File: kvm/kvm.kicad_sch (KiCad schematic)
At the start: 37 parts, among them J1 USB_C_Receptacle_USB2.0, J2 USB_C_Receptacle_USB2.0, SW1 SW_DPDT_x2, U1 FSUSB42MUX, U2 LTC4412xS6, U3 GL850G, U4 L78L33_SOT89, U5 SRV05-4

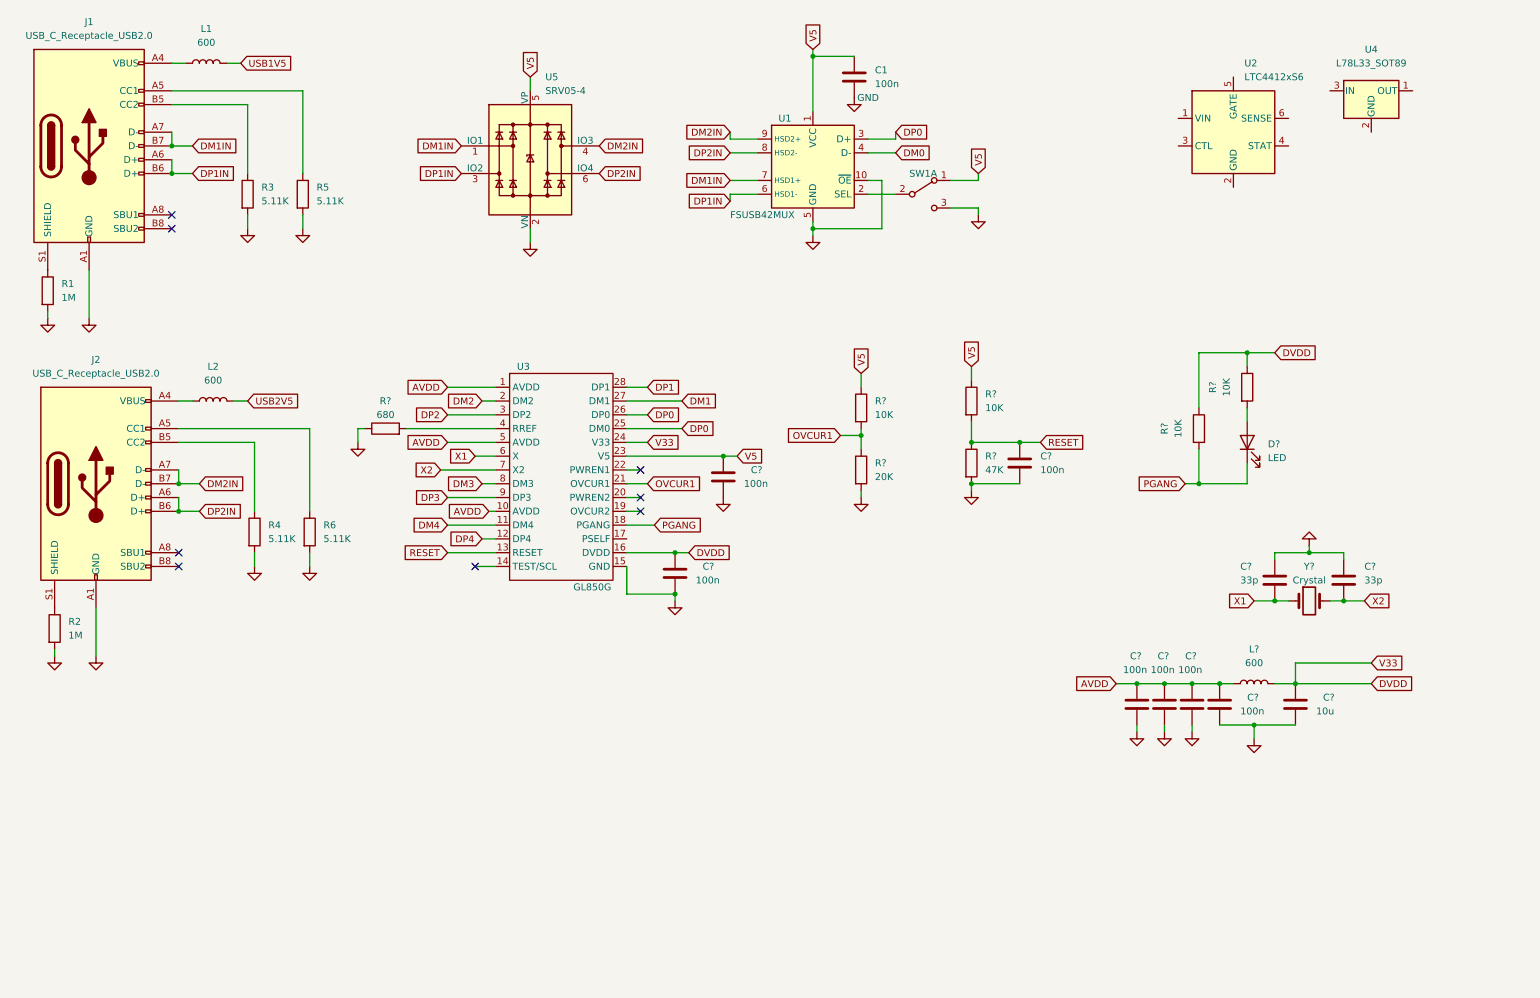
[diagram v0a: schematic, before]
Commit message: SCH: output side finished
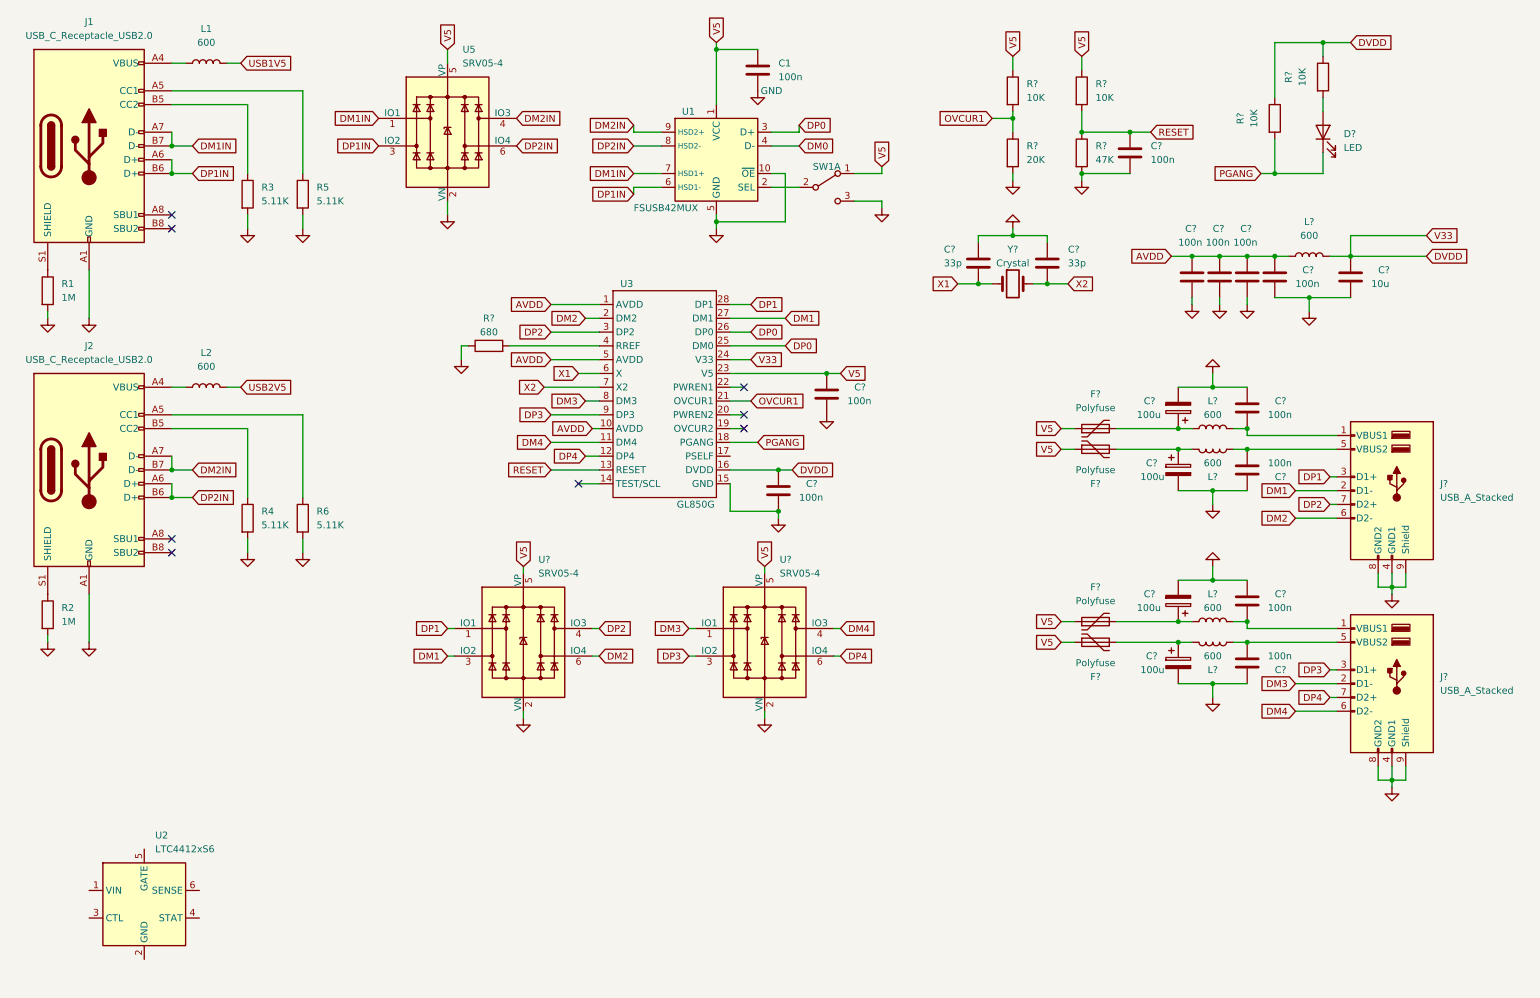
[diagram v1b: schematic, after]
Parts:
- removed U4: L78L33_SOT89, Package_TO_SOT_SMD:SOT-89-3, symbol Regulator_Linear:L78L33_SOT89
- added C? (x4): 100n, Capacitor_SMD:C_0603_1608Metric_Pad1.08x0.95mm_HandSolder, symbol Device:C
- added C? (x4): 100u, Capacitor_THT:CP_Radial_D5.0mm_P2.00mm, symbol Device:C_Polarized
- added F? (x4): Polyfuse, Fuse:Fuse_1206_3216Metric_Pad1.42x1.75mm_HandSolder, symbol Device:Polyfuse
- added J? (x2): USB_A_Stacked, symbol Connector:USB_A_Stacked
- added L? (x4): 600, Resistor_SMD:R_0603_1608Metric_Pad0.98x0.95mm_HandSolder, symbol Device:L
- added U? (x2): SRV05-4, Package_TO_SOT_SMD:SOT-23-6, symbol Power_Protection:SRV05-4
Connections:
- net DM1: now also J?.2 (D1-), U?.3 (IO2)
- net DM2: now also J?.6 (D2-), U?.6 (IO4)
- net DM3: now also J?.2 (D1-), U?.1 (IO1)
- net DM4: now also J?.6 (D2-), U?.4 (IO3)
- net DP1: now also J?.3 (D1+), U?.1 (IO1)
- net DP2: now also J?.7 (D2+), U?.4 (IO3)
- net DP3: now also J?.3 (D1+), U?.3 (IO2)
- net DP4: now also J?.7 (D2+), U?.6 (IO4)
- net GND: now also C?.1, C?.1, C?.1, C?.1, C?.2, C?.2, C?.2, C?.2, J?.4 (GND1), J?.4 (GND1), J?.8 (GND2), J?.8 (GND2), J?.9 (Shield), J?.9 (Shield), U?.2 (VN), U?.2 (VN)
- net V5: now also F?.1, F?.1, F?.1, F?.1, U?.5 (VP), U?.5 (VP)
- new net: C?.1, F?.2, L?.1 (x4)
- new net: C?.2, J?.1 (VBUS1), L?.2 (x2)
- new net: C?.2, J?.5 (VBUS2), L?.2 (x2)
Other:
- moved on the sheet: C1, C?, D?, J2, L2, L?, R2, R4, R6, R?, SW1A, U1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

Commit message: schematic done, footprints missing
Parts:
- added C2: 100u, Capacitor_THT:CP_Radial_D5.0mm_P2.00mm, symbol Device:C_Polarized
- added C3: 100n, Capacitor_SMD:C_0603_1608Metric_Pad1.08x0.95mm_HandSolder, symbol Device:C
- added D1: D_Schottky, Diode_SMD:D_SOD-123F, symbol Device:D_Schottky
- added M1: MPMOS, Package_TO_SOT_SMD:SOT-23-3, symbol pspice:MPMOS
- J1, J2: footprint (none) -> Connector_USB:USB_C_Receptacle_GCT_USB4085
- J3, J4: renamed from J?; footprint (none) -> Connector_USB:USB_A_Wuerth_61400826021_Horizontal_Stacked
- R12: renamed from R?; value 10K -> 100k
- R13: renamed from R?; value 10K -> 780
- SW1: footprint (none) -> Connector_PinHeader_2.54mm:PinHeader_1x03_P2.54mm_Vertical
- gave numbers to parts that had none: 36
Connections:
- net GND: now also U2.2 (GND), U2.3 (CTL), C2.2, C3.1
- net USB1V5: now also D1.2 (A)
- net USB2V5: now also U2.1 (VIN), M1.1 (D)
- net V5: now also U2.6 (SENSE), U3.17 (PSELF), C2.1, C3.2, D1.1 (K), M1.3 (S), M1.4 (B)
- net at U2.5 (GATE): now also M1.2 (G)
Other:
- moved on the sheet: U2

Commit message: finished schematic
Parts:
- removed M1: MPMOS, Package_TO_SOT_SMD:SOT-23-3, symbol pspice:MPMOS
- added Q1: Q_PMOS_GSD, Package_TO_SOT_SMD:SOT-23-3, symbol Device:Q_PMOS_GSD
- added R14: 470K, Resistor_SMD:R_0603_1608Metric_Pad0.98x0.95mm_HandSolder, symbol Device:R
- U3: footprint (none) -> Package_SO:SSOP-28_5.3x10.2mm_P0.65mm
- Y1: footprint (none) -> Library:ECS120184XCKM
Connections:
- net DM0: now also U3.25 (DM0)
- net DM1IN: now also U1.6 (HSD1-); no longer U1.7 (HSD1+)
- net DM2IN: now also U1.8 (HSD2-); no longer U1.9 (HSD2+)
- net DP0: no longer U3.25 (DM0)
- net DP1IN: now also U1.7 (HSD1+); no longer U1.6 (HSD1-)
- net DP2IN: now also U1.9 (HSD2+); no longer U1.8 (HSD2-)
- net USB2V5: now also Q1.3 (D)
- net V5: now also Q1.2 (S), R14.2
- net at U2.4 (STAT): now also R14.1
- net gate: now reaches U2.5 (GATE)
- net gate: now also Q1.1 (G)

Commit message: first layout version
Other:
- moved on the sheet: U4, U6

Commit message: first pcb layout
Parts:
- renumbered C3 to C1, C5 to C10, C4 to C11, C20 to C12, C8 to C13, C18 to C14, C19 to C15, C12 to C16, C11 to C17, C6 to C18, C13 to C19, C1 to C2, C7 to C20, C14 to C21, C2 to C3, C10 to C4, C17 to C5, C9 to C6, C16 to C7, C15 to C8, C21 to C9, F2 to F1, F1 to F2, F4 to F3, F3 to F4, L7 to L5, L5 to L7, R6 to R1, R4 to R10, R7 to R11, R10 to R13, R11 to R14, R14 to R2, R5 to R3, R1 to R4, R2 to R5, R3 to R6, R8 to R7, R9 to R8, R13 to R9, U5 to U2, U2 to U3, U3 to U4, U4 to U5
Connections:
- net DM0 renamed D0-
- net DM1 renamed D1-
- net DM1IN renamed D1IN-
- net DM2 renamed D2-
- net DM2IN renamed D2IN-
- net DM3 renamed D3-
- net DM4 renamed D4-
- net DP0 renamed D0+
- net DP1 renamed D1+
- net DP1IN renamed D1IN+
- net DP2 renamed D2+
- net DP2IN renamed D2IN+
- net DP3 renamed D3+
- net DP4 renamed D4+

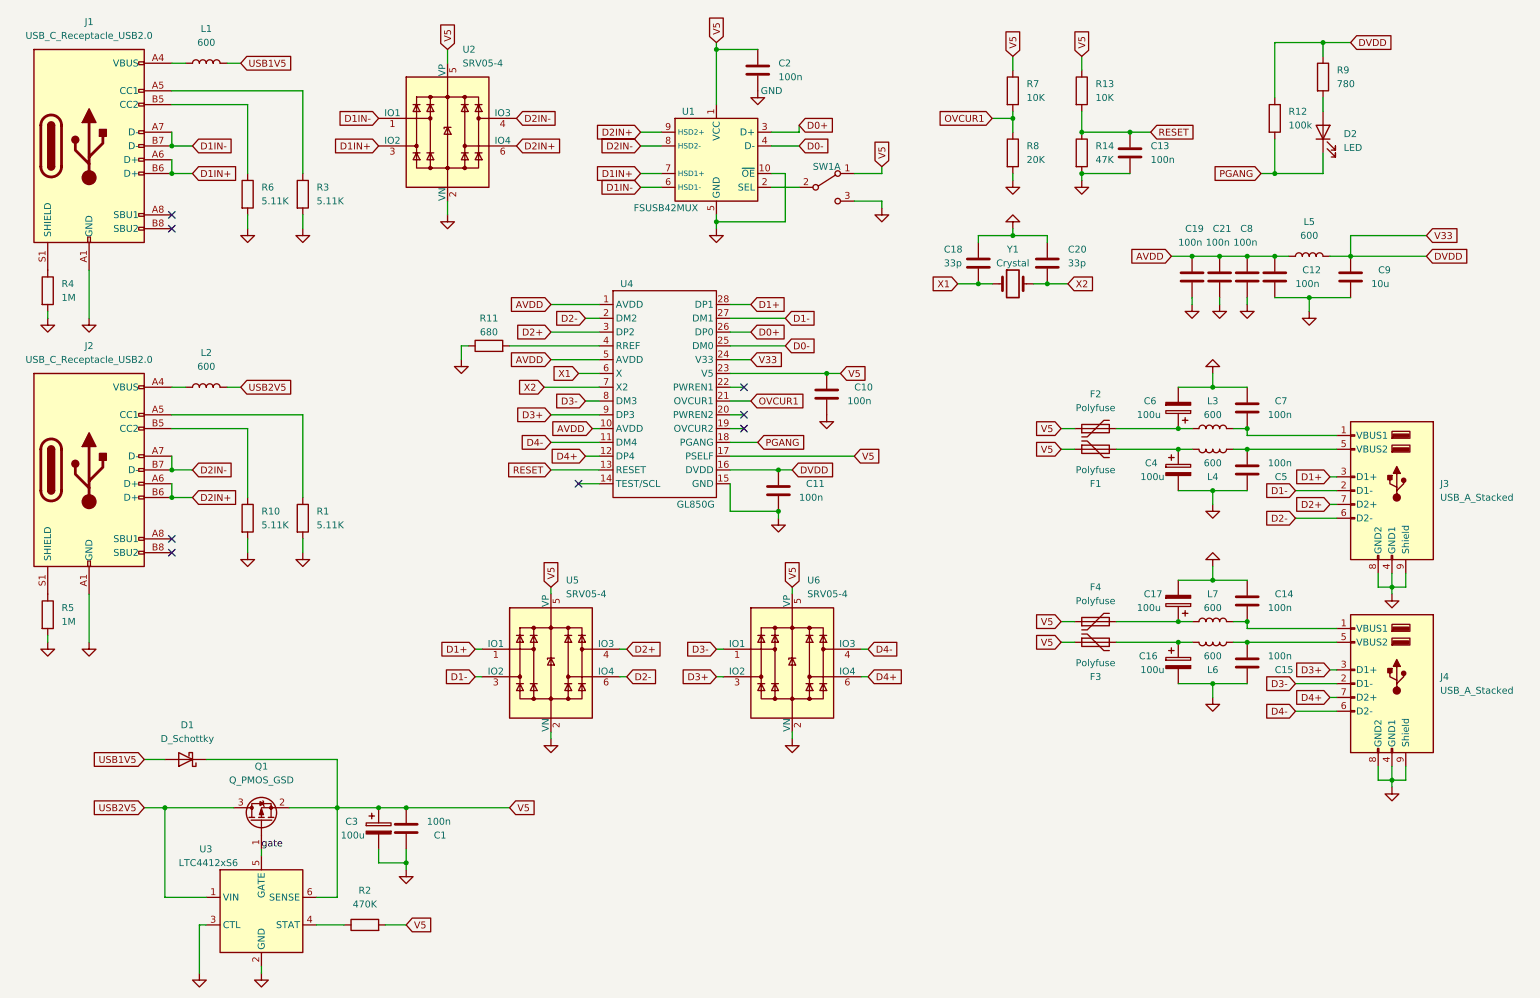
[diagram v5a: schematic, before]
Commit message: replaced USB-C ports with smd parts
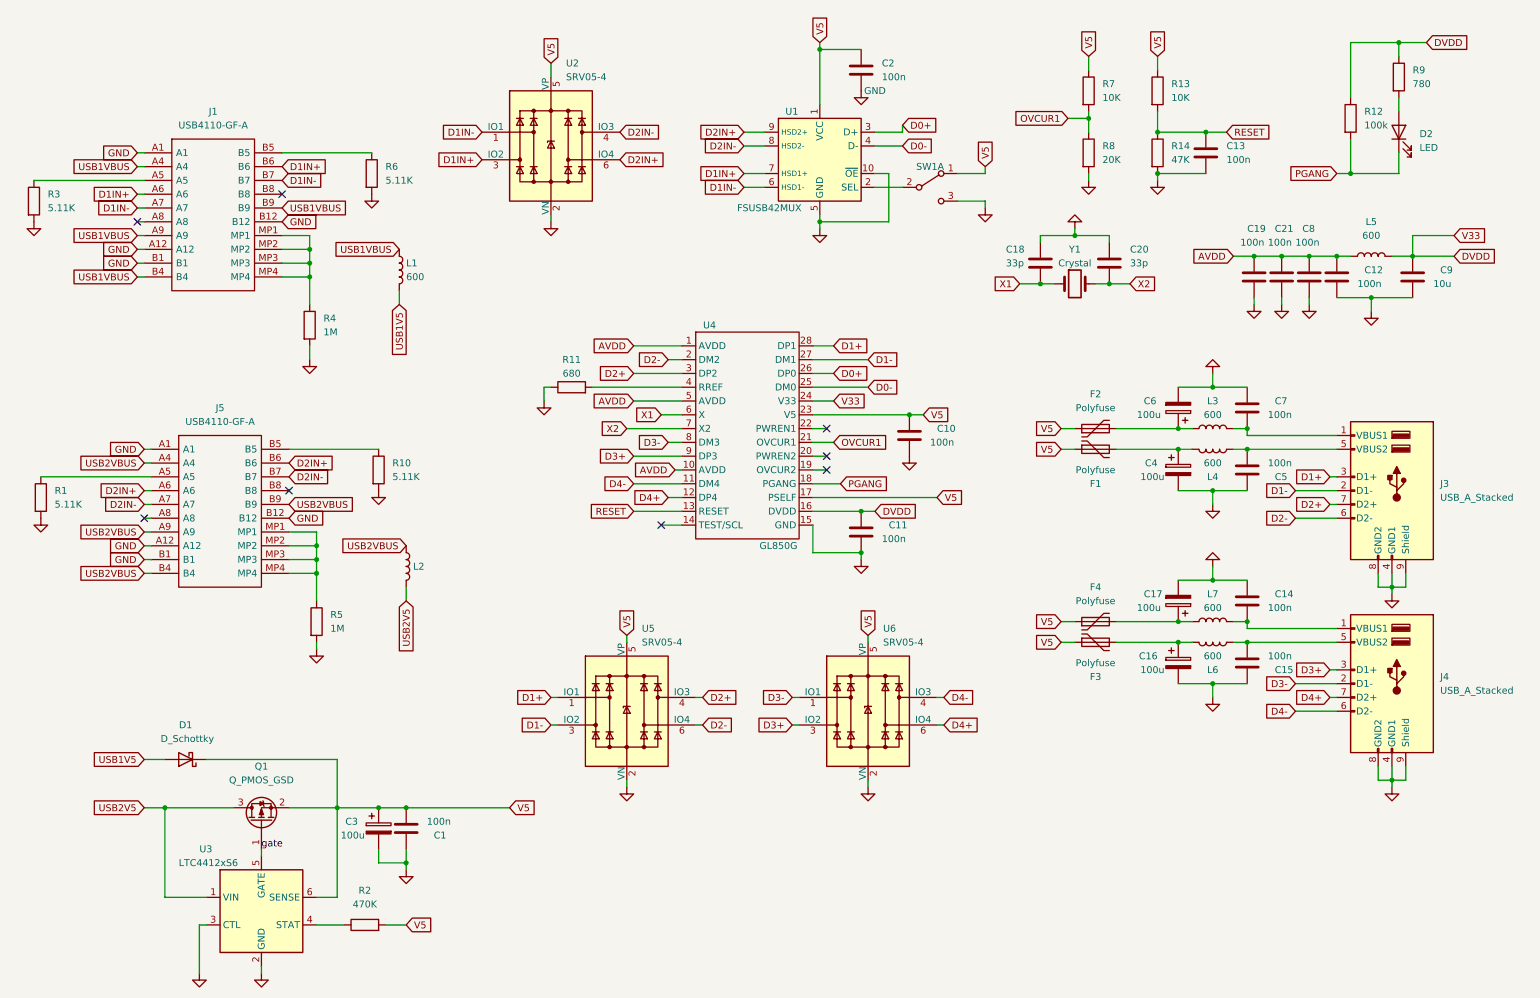
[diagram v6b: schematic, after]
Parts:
- removed J1, J2: USB_C_Receptacle_USB2.0, Connector_USB:USB_C_Receptacle_GCT_USB4085, symbol Connector:USB_C_Receptacle_USB2.0
- added J1, J5: USB4110-GF-A, USB4110GFA, symbol KVM_Library:USB4110-GF-A
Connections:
- net D1IN+: now also J1.A6, J1.B6
- net D1IN-: now also J1.A7, J1.B7
- net D2IN+: now also J5.A6, J5.B6
- net D2IN-: now also J5.A7, J5.B7
- net GND: now also J1.A1, J1.A12, J1.B1, J1.B12, J5.A1, J5.A12, J5.B1, J5.B12
- net at R4.1: now also J1.MP1, J1.MP2, J1.MP3, J1.MP4
- net USB2VBUS: now reaches L2.1
- net USB2VBUS: now also J5.A4, J5.A9, J5.B4, J5.B9
- net at R1.1: now also J5.A5
- net at R10.1: now also J5.B5
- net at R5.1: now also J5.MP1, J5.MP2, J5.MP3, J5.MP4
- net USB1VBUS: now reaches L1.1
- net USB1VBUS: now also J1.A4, J1.A9, J1.B4, J1.B9
- net at R3.1: now also J1.A5
- net at R6.1: now also J1.B5
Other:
- moved on the sheet: C10, C11, C12, C13, C18, C19, C2, C20, C21, C8, C9, D2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

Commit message: reanotated on pcb
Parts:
- J1: renamed from J5; footprint USB4110GFA -> Library:USB4110GFA
- J2: renamed from J1; footprint USB4110GFA -> Library:USB4110GFA
- renumbered C3 to C1, C9 to C10, C8 to C11, C16 to C15, C17 to C16, C15 to C17, C19 to C18, C18 to C19, C1 to C3, C7 to C4, C4 to C6, C6 to C7, C10 to C8, C11 to C9, L7 to L6, L6 to L7, R5 to R10, R12 to R11, R11 to R12, R3 to R2, R2 to R3, R6 to R4, R4 to R5, R7 to R6, R8 to R7, R9 to R8, R10 to R9, U2 to U1, U3 to U2, U1 to U3
